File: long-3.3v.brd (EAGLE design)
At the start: 50 x 50 mm, 37 parts, among them U1 USD-SOCKET, U2 MCP73831, U4 ADXL375BCCZ, X1 Micro USB, X2 CRYSTAL

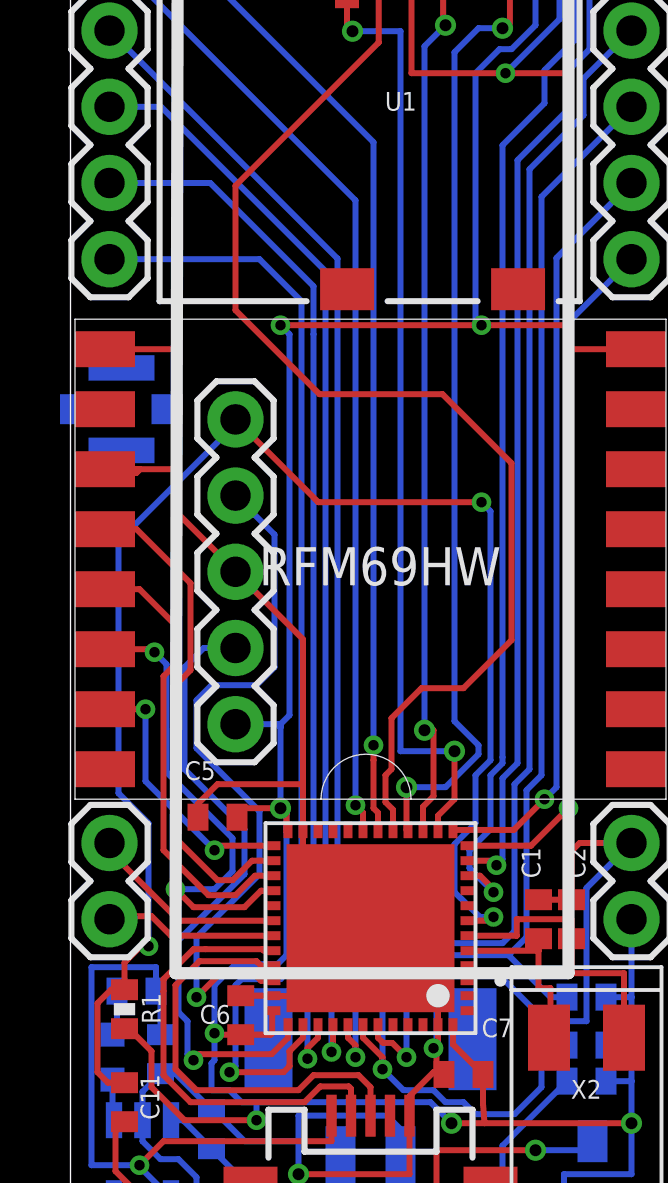
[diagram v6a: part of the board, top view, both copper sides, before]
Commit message: fixed pins and added silk text
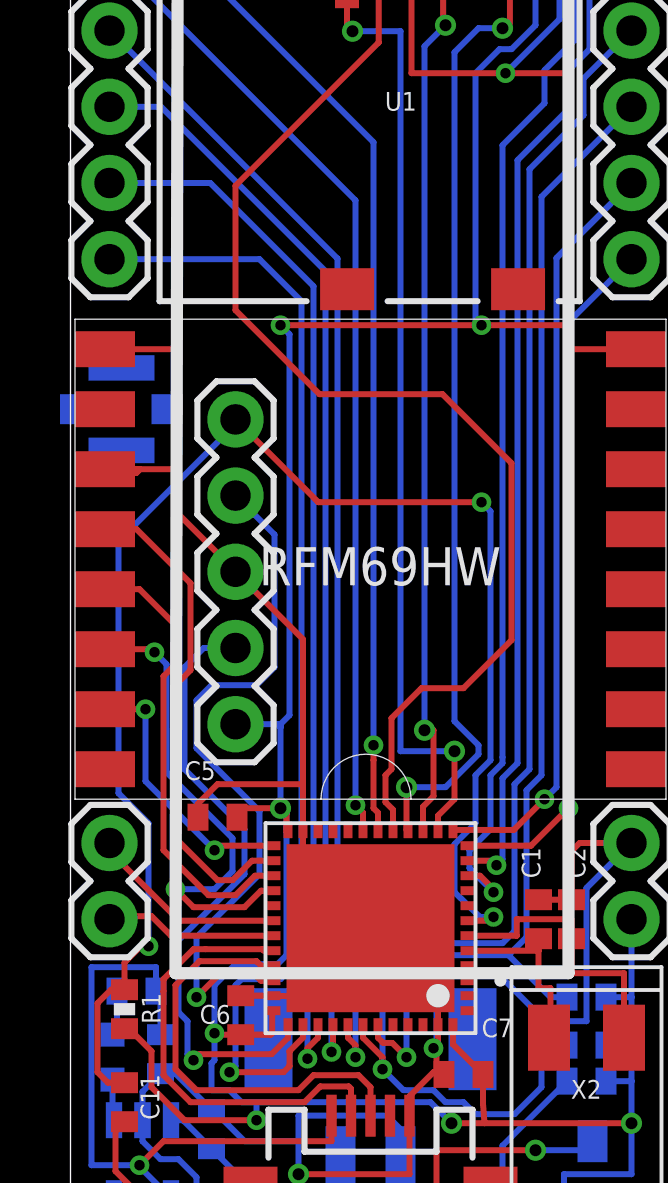
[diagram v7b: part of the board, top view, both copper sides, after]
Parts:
- D11: value RED -> POWER
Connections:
- new net CS: JP10.1, U$1.P$38
- new net GPIO1: JP12.6
- new net GPIO2: JP12.5
- new net GPIO3: JP13.6
- new net GPIO4: JP13.5
- new net I2C_SCL: JP12.4
- new net I2C_SDA: JP12.3
- new net MISO: JP10.3, U$1.P$40
- new net MOSI: JP10.4, U$1.P$41
- new net RX2: JP14.1
- new net SCK: JP10.2, U$1.P$39
- new net TX2: JP14.2
- new net UART_RX: JP12.2
- new net UART_TX: JP12.1
- net FC_RX: no longer JP16.1
- net FC_TX: no longer JP16.2
- net GPS_RX: now also JP16.2; no longer JP14.2
- net GPS_TX: now also JP16.1; no longer JP14.1
- net PA0: no longer JP12.6
- net PA1: no longer JP12.5
- net PB0: no longer JP13.6
- net PB1: no longer JP13.5
- net RX: no longer JP12.2
- net SCL: no longer JP12.4
- net SDA: no longer JP12.3
- net SPI_CS: no longer JP10.1, U$1.P$38
- net SPI_MISO: no longer JP10.3, U$1.P$40
- net SPI_MOSI: no longer JP10.4, U$1.P$41
- net SPI_SCK: no longer JP10.2, U$1.P$39
- net TX: no longer JP12.1
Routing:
- net SPI_MOSI: track 38.8 -> 0.00 mm, vias 1 -> 0
- net MOSI: track 0.00 -> 38.8 mm, vias 0 -> 1
- net SPI_CS: track 38.0 -> 0.00 mm, vias 1 -> 0
- net CS: track 0.00 -> 38.0 mm, vias 0 -> 1
- net SPI_MISO: track 36.4 -> 0.00 mm, vias 1 -> 0
- net MISO: track 0.00 -> 36.4 mm, vias 0 -> 1
- net SCK: track 0.00 -> 35.3 mm, vias 0 -> 1
- net SPI_SCK: track 35.3 -> 0.00 mm, vias 1 -> 0
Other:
- board text added: "3.3V"
- board text added: "CS"
- board text added: "GND"
- board text added: "GPS_RX"
- board text added: "GPS_TX"
- board text added: "MISO"
- board text added: "MOSI"
- board text added: "PA0"
- board text added: "PA1"
- board text added: "PB0"
- board text added: "PB1"
- board text added: "RX"
- board text added: "RX2"
- board text added: "SCK"
- board text added: "SCL"
- board text added: "SDA"
- board text added: "TX"
- board text added: "TX2"

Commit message: connected antenna. NRST needs rerouting.
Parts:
- moved JP1 1.61 mm to (5.70, 20.1)
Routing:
- net N$4: track 0.00 -> 4.43 mm, vias 0 -> 1
- net NRST: track 51.4 -> 53.6 mm
- net SWDIO: track 23.9 -> 25.6 mm
- net SWCLK: track 20.8 -> 21.9 mm
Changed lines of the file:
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@@
 <element name="JP16" library="SparkFun-Connectors" package="1X02" value="M02PTH" x="31.7" y="12" smashed="yes" rot="R90"/>
 <element name="JP17" library="SparkFun-Connectors" package="1X02" value="M02PTH" x="48.7" y="12" smashed="yes" rot="R90"/>
-<element name="JP1" library="SparkFun" package="1X05" value="" x="5.5" y="18.5" smashed="yes" rot="R90">
-<attribute name="VALUE" x="8.675" y="17.23" size="1.27" layer="27" rot="R90"/>
+<element name="JP1" library="SparkFun" package="1X05" value="" x="5.7" y="20.1" smashed="yes" rot="R90">
+<attribute name="VALUE" x="8.875" y="18.83" size="1.27" layer="27" rot="R90"/>
 </element>
 <element name="R1" library="SparkFun" package="0402-RES" value="10k" x="1.8" y="9" smashed="yes" rot="R90">
@@
 <contactref element="JP1" pad="3"/>
 <contactref element="C11" pad="2"/>
-<wire x1="5.5" y1="23.58" x2="5.5" y2="23.6" width="0.2" layer="1"/>
-<wire x1="5.5" y1="23.6" x2="3.6" y2="25.5" width="0.2" layer="1"/>
-<wire x1="3.6" y1="25.5" x2="3.6" y2="27" width="0.2" layer="1"/>
 <wire x1="3.6" y1="27" x2="2.32" y2="27" width="0.2" layer="1"/>
 <wire x1="2.32" y1="27" x2="2.2" y2="26.88" width="0.2" layer="1"/>
 <wire x1="2.2" y1="26.88" x2="2.2" y2="27" width="0.2" layer="1"/>
-<wire x1="7.75" y1="16.5" x2="7.75" y2="21.33" width="0.2" layer="1"/>
-<wire x1="7.75" y1="21.33" x2="5.5" y2="23.58" width="0.2" layer="1"/>
+<wire x1="7.75" y1="16.5" x2="7.75" y2="23.13" width="0.2" layer="1"/>
+<wire x1="7.75" y1="23.13" x2="5.7" y2="25.18" width="0.2" layer="1"/>
 <wire x1="1.8" y1="5.25" x2="1.5" y2="4.95" width="0.2" layer="1"/>
 <wire x1="1.5" y1="4.95" x2="1.5" y2="3.6" width="0.2" layer="1"/>
@@
 <contactref element="U$4" pad="P$2"/>
 <contactref element="U$4" pad="P$1"/>
+<wire x1="3.6" y1="27" x2="5.42" y2="25.18" width="0.2" layer="1"/>
+<wire x1="5.42" y1="25.18" x2="5.7" y2="25.18" width="0.2" layer="1"/>
 <wire x1="39.1291125" y1="24.4" x2="39.1291125" y2="25.999996875" width="0" layer="19" extent="1-1"/>
 <wire x1="39.1291125" y1="23.600003125" x2="39.1291125" y2="24.4" width="0" layer="19" extent="1-1"/>
@@
 <wire x1="5.5" y1="10.5" x2="6.9" y2="10.5" width="0.2" layer="16"/>
 <wire x1="6.9" y1="10.5" x2="7.2" y2="10.8" width="0.2" layer="16"/>
-<wire x1="7" y1="15.7" x2="7" y2="18.4" width="0.2" layer="16"/>
-<wire x1="7" y1="18.4" x2="7" y2="18.5" width="0.2" layer="16"/>
-<wire x1="7" y1="18.5" x2="7.3" y2="18.8" width="0.2" layer="16"/>
-<wire x1="7.3" y1="18.8" x2="7.3" y2="31.5" width="0.2" layer="16"/>
+<wire x1="7" y1="15.7" x2="7" y2="18.8" width="0.2" layer="16"/>
+<wire x1="7.3" y1="19.1" x2="7.3" y2="31.5" width="0.2" layer="16"/>
 <wire x1="7.3" y1="31.5" x2="7" y2="31.8" width="0.2" layer="16"/>
 <wire x1="5.8" y1="47.7" x2="10.5" y2="47.7" width="0.2" layer="16"/>
@@
 <contactref element="JP1" pad="1"/>
 <contactref element="R1" pad="1"/>
-<wire x1="5.5" y1="18.5" x2="6.9" y2="18.5" width="0.2" layer="16"/>
-<wire x1="6.9" y1="18.5" x2="7" y2="18.4" width="0.2" layer="16"/>
 <wire x1="4.7" y1="6.3" x2="4.7" y2="7.2" width="0.2" layer="16"/>
 <wire x1="4.7" y1="7.2" x2="4.8" y2="7.3" width="0.2" layer="16"/>
@@
 <wire x1="17.85" y1="7.8" x2="18.7" y2="7.8" width="0.2" layer="16"/>
 <wire x1="17.85" y1="9.4" x2="18.7" y2="9.4" width="0.2" layer="16"/>
+<wire x1="7" y1="18.8" x2="5.7" y2="20.1" width="0.2" layer="16"/>
+<wire x1="7" y1="18.8" x2="7.3" y2="19.1" width="0.2" layer="16"/>
 <wire x1="39.1291125" y1="22.800003125" x2="39.1291125" y2="26.799996875" width="0" layer="19" extent="1-1"/>
 <wire x1="40.35" y1="18.15" x2="39.1291125" y2="22.800003125" width="0" layer="19" extent="1-1"/>
@@
 <wire x1="6.3" y1="13.5" x2="6.3" y2="15.6" width="0.2" layer="16"/>
 <wire x1="6.3" y1="15.6" x2="4.2" y2="17.7" width="0.2" layer="16"/>
-<wire x1="4.2" y1="17.7" x2="4.2" y2="19.3" width="0.2" layer="16"/>
-<wire x1="4.2" y1="19.3" x2="4.7" y2="19.8" width="0.2" layer="16"/>
-<wire x1="4.7" y1="19.8" x2="6.2" y2="19.8" width="0.2" layer="16"/>
-<wire x1="6.2" y1="19.8" x2="6.8" y2="20.4" width="0.2" layer="16"/>
-<wire x1="6.8" y1="20.4" x2="6.8" y2="24.82" width="0.2" layer="16"/>
-<wire x1="6.8" y1="24.82" x2="5.5" y2="26.12" width="0.2" layer="16"/>
+<wire x1="4.2" y1="17.7" x2="4.2" y2="20.6" width="0.2" layer="16"/>
+<wire x1="4.2" y1="20.6" x2="4.9" y2="21.3" width="0.2" layer="16"/>
+<wire x1="4.9" y1="21.3" x2="6.5" y2="21.3" width="0.2" layer="16"/>
+<wire x1="6.5" y1="21.3" x2="6.9" y2="21.7" width="0.2" layer="16"/>
+<wire x1="6.9" y1="21.7" x2="6.9" y2="26.52" width="0.2" layer="16"/>
+<wire x1="6.9" y1="26.52" x2="5.7" y2="27.72" width="0.2" layer="16"/>
 </signal>
 <signal name="SWCLK">
 <contactref element="U$1" pad="P$37"/>
 <contactref element="JP1" pad="2"/>
-<wire x1="3.8" y1="20.4" x2="3.8" y2="17" width="0.2" layer="16"/>
+<wire x1="3.8" y1="20.74" x2="3.8" y2="17" width="0.2" layer="16"/>
 <wire x1="3.8" y1="17" x2="5.8" y2="15" width="0.2" layer="16"/>
 <wire x1="5.8" y1="15" x2="5.8" y2="13.5" width="0.2" layer="16"/>
@@
 <wire x1="6.7" y1="7.5" x2="7.25" y2="8.05" width="0.2" layer="1"/>
 <wire x1="7.25" y1="8.05" x2="7.25" y2="8.425" width="0.2" layer="1"/>
-<wire x1="5.5" y1="21.04" x2="4.44" y2="21.04" width="0.2" layer="16"/>
-<wire x1="4.44" y1="21.04" x2="3.8" y2="20.4" width="0.2" layer="16"/>
+<wire x1="3.8" y1="20.74" x2="5.7" y2="22.64" width="0.2" layer="16"/>
 </signal>
 <signal name="PB1">
@@
 <wire x1="14" y1="25.6" x2="13.7" y2="25.9" width="0.2" layer="16"/>
 <via x="13.7" y="25.9" extent="1-16" drill="0.35"/>
-<wire x1="13.7" y1="25.9" x2="8.26" y2="25.9" width="0.2" layer="1"/>
-<wire x1="8.26" y1="25.9" x2="5.5" y2="28.66" width="0.2" layer="1"/>
-<wire x1="5.5" y1="28.66" x2="5.5" y2="28.5" width="0.2" layer="16"/>
-<wire x1="5.5" y1="28.5" x2="1.6" y2="24.6" width="0.2" layer="16"/>
+<wire x1="13.7" y1="25.9" x2="10.06" y2="25.9" width="0.2" layer="1"/>
+<wire x1="10.06" y1="25.9" x2="5.7" y2="30.26" width="0.2" layer="1"/>
 <wire x1="1.6" y1="24.6" x2="1.6" y2="16.2" width="0.2" layer="16"/>
 <wire x1="1.6" y1="16.2" x2="2.6" y2="15.2" width="0.2" layer="16"/>
@@
 <wire x1="0.9" y1="9.2" x2="1.35" y2="9.65" width="0.2" layer="1"/>
 <wire x1="1.35" y1="9.65" x2="1.8" y2="9.65" width="0.2" layer="1"/>
+<wire x1="1.6" y1="24.6" x2="4.2" y2="27.2" width="0.2" layer="16"/>
+<wire x1="4.2" y1="27.2" x2="4.2" y2="28" width="0.2" layer="16"/>
+<wire x1="4.2" y1="28" x2="5.7" y2="29.5" width="0.2" layer="16"/>
+<wire x1="5.7" y1="29.5" x2="5.7" y2="30.26" width="0.2" layer="16"/>
 </signal>
 <signal name="N$4">
 <contactref element="U$4" pad="P$3"/>
 <contactref element="U$3" pad="ANT"/>
-<wire x1="1.15" y1="29" x2="3.225" y2="29" width="0" layer="19" extent="1-16"/>
+<wire x1="1.15" y1="29" x2="4.4" y2="29" width="1.2" layer="1"/>
+<via x="4.4" y="29" extent="1-16" drill="0.35"/>
+<wire x1="4.4" y1="29" x2="3.225" y2="29" width="1" layer="16"/>
 </signal>
 <signal name="RX2">
